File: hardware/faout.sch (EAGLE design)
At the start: 163 parts, among them IC2 MT48LC8M16A2, Q1 L7912ACV, Q2 12MHz, Q3 MUN2214T1, Q4 MUN2214T1, Q5 ASFL, SW1 SMD_TACT_SWITCH, SW2 SMD_TACT_SWITCH, SW3 SMD_TACT_SWITCH, U1 93LC46BT-I/OT, U10 DAC8811DGK, U11 REF102AU, U12 DAC8811DGK, U13 ADR435ARZ, U14 AD8627AKSZ-R2, U15 OPA2277UA/2K5E4, U16 OPA2277UA/2K5E4, U17 MCP1700T-2502E/TT, U18 AD7980ARMZ, U2 LM3480IM3-3.3, U3 LM2940T-12.0, U4 LM3671MF-3.3, U5 LM3671MF-1.2, U6 FLASH-SPI-25XXSMD1, U7 6SLX9TQG144, U8 AD8220ARMZ, U9 REF102AU

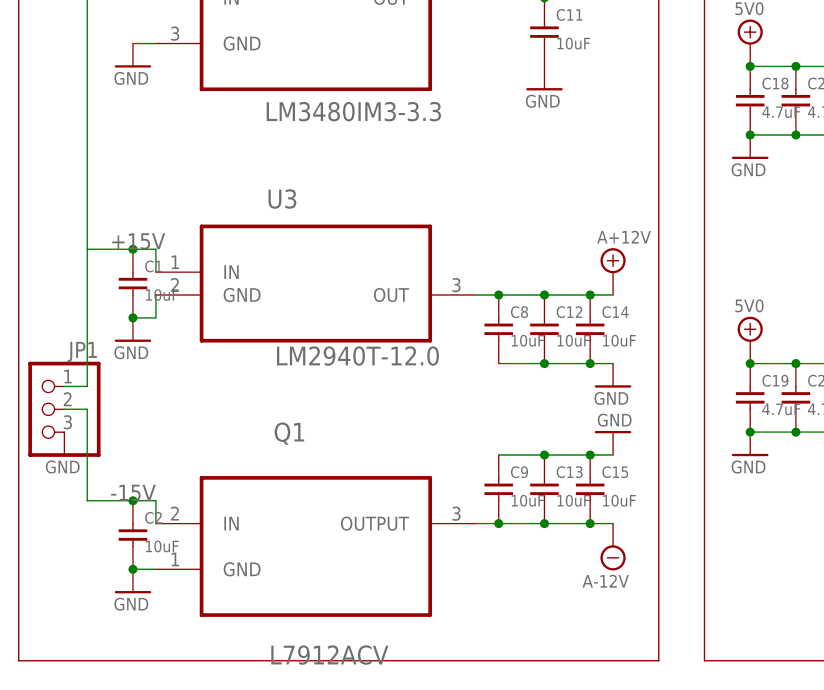
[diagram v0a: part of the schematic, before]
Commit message: Unify analog regulators.
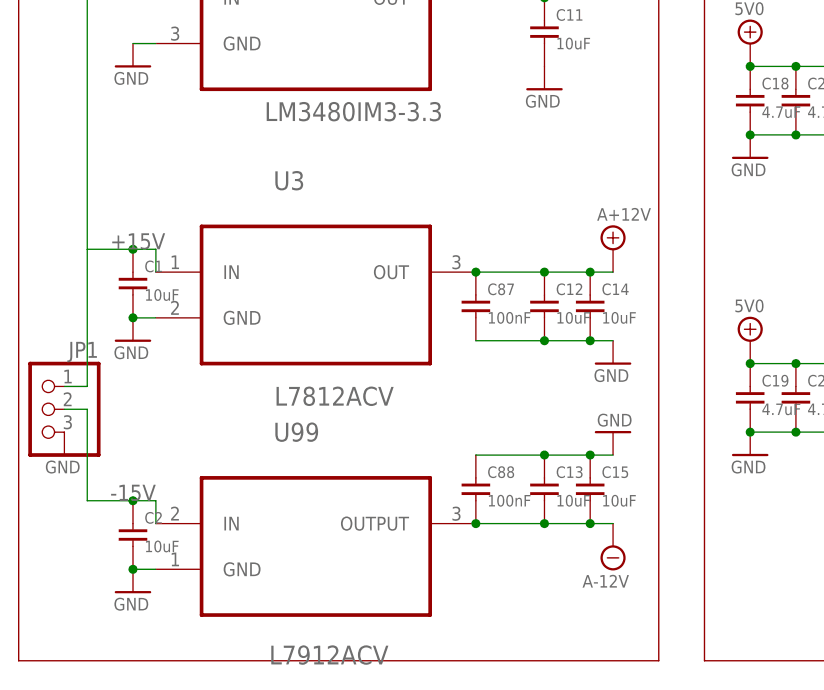
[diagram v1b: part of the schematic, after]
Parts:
- removed C8, C9: 10uF, faout:C_EU0805
- added C87, C88: 100nF, faout:C_EU0603
- U3: value LM2940T-12.0 -> L7812ACV; device faout:LM2940T-12.0 -> faout:L7812ACV
- renumbered Q1 to U99
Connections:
- net A+12V: now also C87.P$1; no longer C8.P$1
- net A-12V: now also C88.P$2; no longer C9.P$2
- net GND: now also C87.P$2, C88.P$1; no longer C8.P$2, C9.P$1
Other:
- moved on the sheet: C12, C14, U3
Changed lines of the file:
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@@
 </part>
 <part name="JP1" library="pinhead" deviceset="PINHD-1X3" device=""/>
-<part name="U3" library="faout" deviceset="LM2940T-12.0" device=""/>
-<part name="Q1" library="faout" deviceset="L7912ACV" device=""/>
+<part name="U3" library="faout" deviceset="L7812ACV" device=""/>
+<part name="U99" library="faout" deviceset="L7912ACV" device=""/>
 <part name="A+12V_PWR7" library="faout" deviceset="A+12V" device=""/>
 <part name="U$1" library="faout" deviceset="A-12V" device=""/>
@@
 <attribute name="OC_FARNELL" value="1867958"/>
 </part>
-<part name="C8" library="faout" deviceset="C_EU" device="0805" value="10uF">
-<attribute name="OC_FARNELL" value="1867958"/>
-</part>
 <part name="C14" library="faout" deviceset="C_EU" device="0805" value="10uF">
 <attribute name="OC_FARNELL" value="1867958"/>
 </part>
-<part name="C9" library="faout" deviceset="C_EU" device="0805" value="10uF">
-<attribute name="OC_FARNELL" value="1867958"/>
-</part>
 <part name="C13" library="faout" deviceset="C_EU" device="0805" value="10uF">
 <attribute name="OC_FARNELL" value="1867958"/>
@@
 <part name="GND_PWR80" library="Bogdan_Commons" deviceset="GND" device=""/>
 <part name="U1" library="faout" deviceset="93LC46BT-I/OT" device=""/>
+<part name="C87" library="faout" deviceset="C_EU" device="0603" value="100nF">
+<attribute name="OC_FARNELL" value="1740621"/>
+</part>
+<part name="C88" library="faout" deviceset="C_EU" device="0603" value="100nF">
+<attribute name="OC_FARNELL" value="1740621"/>
+</part>
 </parts>
 <sheets>
@@
 </instance>
 <instance part="JP1" gate="A" x="-20.32" y="2.54" rot="MR0"/>
-<instance part="U3" gate="A" x="10.16" y="20.32"/>
-<instance part="Q1" gate="A" x="10.16" y="-10.16"/>
-<instance part="A+12V_PWR7" gate="G$1" x="43.18" y="17.78"/>
+<instance part="U3" gate="A" x="10.16" y="17.78"/>
+<instance part="U99" gate="A" x="10.16" y="-10.16"/>
+<instance part="A+12V_PWR7" gate="G$1" x="43.18" y="20.32"/>
 <instance part="U$1" gate="G$1" x="43.18" y="-12.7"/>
 <instance part="GND_PWR13" gate="A" x="-17.78" y="-2.54"/>
 <instance part="GND_PWR75" gate="A" x="-10.16" y="-17.78"/>
 <instance part="GND_PWR76" gate="A" x="-10.16" y="10.16"/>
-<instance part="C12" gate="G$1" x="35.56" y="12.7">
-<attribute name="OC_FARNELL" x="35.56" y="12.7" size="1.778" layer="96" display="off"/>
+<instance part="C12" gate="G$1" x="35.56" y="15.24">
+<attribute name="OC_FARNELL" x="35.56" y="15.24" size="1.778" layer="96" display="off"/>
 </instance>
-<instance part="C8" gate="G$1" x="30.48" y="12.7">
-<attribute name="OC_FARNELL" x="30.48" y="12.7" size="1.778" layer="96" display="off"/>
-</instance>
-<instance part="C14" gate="G$1" x="40.64" y="12.7">
-<attribute name="OC_FARNELL" x="40.64" y="12.7" size="1.778" layer="96" display="off"/>
-</instance>
-<instance part="C9" gate="G$1" x="30.48" y="-5.08">
-<attribute name="OC_FARNELL" x="30.48" y="-5.08" size="1.778" layer="96" display="off"/>
+<instance part="C14" gate="G$1" x="40.64" y="15.24">
+<attribute name="OC_FARNELL" x="40.64" y="15.24" size="1.778" layer="96" display="off"/>
 </instance>
 <instance part="C13" gate="G$1" x="35.56" y="-5.08">
@@
 <attribute name="OC_FARNELL" x="-10.16" y="-10.16" size="1.778" layer="96" display="off"/>
 </instance>
-<instance part="GND_PWR77" gate="A" x="43.18" y="5.08"/>
+<instance part="GND_PWR77" gate="A" x="43.18" y="7.62"/>
 <instance part="GND_PWR78" gate="A" x="43.18" y="0" rot="R180"/>
 <instance part="U2" gate="A" x="10.16" y="48.26"/>
@@
 <instance part="GND_PWR80" gate="A" x="35.56" y="38.1"/>
 <instance part="U1" gate="A" x="-2.54" y="-170.18"/>
+<instance part="C87" gate="G$1" x="27.94" y="15.24">
+<attribute name="OC_FARNELL" x="27.94" y="15.24" size="1.778" layer="96" display="off"/>
+</instance>
+<instance part="C88" gate="G$1" x="27.94" y="-5.08">
+<attribute name="OC_FARNELL" x="27.94" y="-5.08" size="1.778" layer="96" display="off"/>
+</instance>
 </instances>
 <busses>
@@
 </segment>
 <segment>
-<pinref part="Q1" gate="A" pin="GND"/>
+<pinref part="U99" gate="A" pin="GND"/>
 <pinref part="GND_PWR75" gate="A" pin="GND"/>
 <wire x1="-10.16" y1="-15.24" x2="-7.62" y2="-15.24" width="0.1524" layer="91"/>
@@
 <pinref part="GND_PWR76" gate="A" pin="GND"/>
 <wire x1="-10.16" y1="12.7" x2="-7.62" y2="12.7" width="0.1524" layer="91"/>
-<wire x1="-7.62" y1="12.7" x2="-7.62" y2="15.24" width="0.1524" layer="91"/>
 <pinref part="C1" gate="G$1" pin="P$2"/>
 <junction x="-10.16" y="12.7"/>
@@
 <segment>
 <pinref part="GND_PWR78" gate="A" pin="GND"/>
-<pinref part="C9" gate="G$1" pin="P$1"/>
 <wire x1="43.18" y1="-2.54" x2="40.64" y2="-2.54" width="0.1524" layer="91"/>
 <pinref part="C13" gate="G$1" pin="P$1"/>
 <junction x="35.56" y="-2.54"/>
 <wire x1="40.64" y1="-2.54" x2="35.56" y2="-2.54" width="0.1524" layer="91"/>
-<wire x1="35.56" y1="-2.54" x2="30.48" y2="-2.54" width="0.1524" layer="91"/>
+<wire x1="35.56" y1="-2.54" x2="27.94" y2="-2.54" width="0.1524" layer="91"/>
 <pinref part="C15" gate="G$1" pin="P$1"/>
 <junction x="40.64" y="-2.54"/>
+<pinref part="C88" gate="G$1" pin="P$1"/>
 </segment>
 <segment>
-<pinref part="C8" gate="G$1" pin="P$2"/>
 <pinref part="GND_PWR77" gate="A" pin="GND"/>
-<wire x1="30.48" y1="7.62" x2="35.56" y2="7.62" width="0.1524" layer="91"/>
+<wire x1="27.94" y1="10.16" x2="35.56" y2="10.16" width="0.1524" layer="91"/>
 <pinref part="C14" gate="G$1" pin="P$2"/>
-<junction x="40.64" y="7.62"/>
-<wire x1="35.56" y1="7.62" x2="40.64" y2="7.62" width="0.1524" layer="91"/>
-<wire x1="40.64" y1="7.62" x2="43.18" y2="7.62" width="0.1524" layer="91"/>
+<junction x="40.64" y="10.16"/>
+<wire x1="35.56" y1="10.16" x2="40.64" y2="10.16" width="0.1524" layer="91"/>
+<wire x1="40.64" y1="10.16" x2="43.18" y2="10.16" width="0.1524" layer="91"/>
 <pinref part="C12" gate="G$1" pin="P$2"/>
-<junction x="35.56" y="7.62"/>
+<junction x="35.56" y="10.16"/>
+<pinref part="C87" gate="G$1" pin="P$2"/>
 </segment>
 <segment>
@@
 <pinref part="U3" gate="A" pin="OUT"/>
 <pinref part="A+12V_PWR7" gate="G$1" pin="A+12V"/>
-<wire x1="27.94" y1="15.24" x2="30.48" y2="15.24" width="0.1524" layer="91"/>
 <pinref part="C12" gate="G$1" pin="P$1"/>
-<wire x1="30.48" y1="15.24" x2="35.56" y2="15.24" width="0.1524" layer="91"/>
-<wire x1="35.56" y1="15.24" x2="40.64" y2="15.24" width="0.1524" layer="91"/>
-<junction x="35.56" y="15.24"/>
-<pinref part="C8" gate="G$1" pin="P$1"/>
-<junction x="30.48" y="15.24"/>
+<wire x1="27.94" y1="17.78" x2="35.56" y2="17.78" width="0.1524" layer="91"/>
+<wire x1="35.56" y1="17.78" x2="40.64" y2="17.78" width="0.1524" layer="91"/>
+<junction x="35.56" y="17.78"/>
 <pinref part="C14" gate="G$1" pin="P$1"/>
-<wire x1="40.64" y1="15.24" x2="43.18" y2="15.24" width="0.1524" layer="91"/>
-<junction x="40.64" y="15.24"/>
+<wire x1="40.64" y1="17.78" x2="43.18" y2="17.78" width="0.1524" layer="91"/>
+<junction x="40.64" y="17.78"/>
+<pinref part="C87" gate="G$1" pin="P$1"/>
+<junction x="27.94" y="17.78"/>
 </segment>
 </net>
@@
 </segment>
 <segment>
-<pinref part="Q1" gate="A" pin="OUTPUT"/>
 <pinref part="U$1" gate="G$1" pin="A-12V"/>
-<wire x1="27.94" y1="-10.16" x2="30.48" y2="-10.16" width="0.1524" layer="91"/>
-<pinref part="C9" gate="G$1" pin="P$2"/>
-<wire x1="30.48" y1="-10.16" x2="35.56" y2="-10.16" width="0.1524" layer="91"/>
-<junction x="30.48" y="-10.16"/>
 <pinref part="C13" gate="G$1" pin="P$2"/>
 <wire x1="35.56" y1="-10.16" x2="40.64" y2="-10.16" width="0.1524" layer="91"/>
-<junction x="35.56" y="-10.16"/>
 <pinref part="C15" gate="G$1" pin="P$2"/>
 <wire x1="40.64" y1="-10.16" x2="43.18" y2="-10.16" width="0.1524" layer="91"/>
 <junction x="40.64" y="-10.16"/>
+<pinref part="U99" gate="A" pin="OUTPUT"/>
+<pinref part="C88" gate="G$1" pin="P$2"/>
+<junction x="27.94" y="-10.16"/>
+<wire x1="27.94" y1="-10.16" x2="35.56" y2="-10.16" width="0.1524" layer="91"/>
+<junction x="35.56" y="-10.16"/>
 </segment>
 </net>
@@
 <wire x1="-17.78" y1="2.54" x2="-15.24" y2="2.54" width="0.1524" layer="91"/>
 <wire x1="-15.24" y1="2.54" x2="-15.24" y2="-7.62" width="0.1524" layer="91"/>
-<pinref part="Q1" gate="A" pin="IN"/>
+<pinref part="U99" gate="A" pin="IN"/>
 <wire x1="-15.24" y1="-7.62" x2="-10.16" y2="-7.62" width="0.1524" layer="91"/>
 <wire x1="-10.16" y1="-7.62" x2="-7.62" y2="-7.62" width="0.1524" layer="91"/>

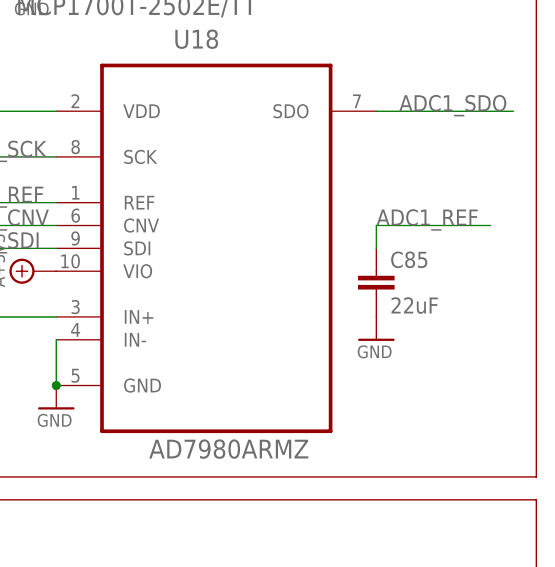
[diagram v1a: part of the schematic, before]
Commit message: Rearrange labels
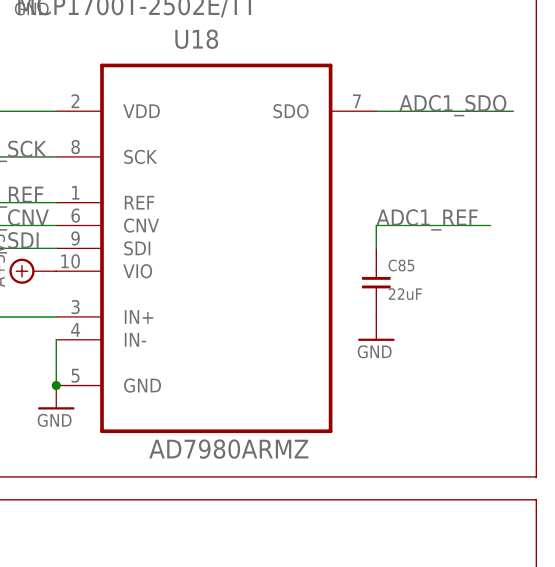
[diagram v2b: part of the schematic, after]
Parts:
- C85: device resistor:C-EUC1206 -> faout:C_EU1206
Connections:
- net ADC1_REF: now also C85.P$1; no longer C85.1
- net GND: now also C85.P$2; no longer C85.2
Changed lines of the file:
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@@
 <part name="U17" library="faout" deviceset="MCP1700T-2502E/TT" device=""/>
 <part name="AI1" library="analog_out_lib" deviceset="BU-SMA" device=""/>
-<part name="C85" library="resistor" deviceset="C-EU" device="C1206" value="22uF"/>
+<part name="C85" library="faout" deviceset="C_EU" device="1206" value="22uF"/>
 <part name="GND_PWR48" library="faout" deviceset="GND" device=""/>
 <part name="GND_PWR49" library="faout" deviceset="GND" device=""/>
@@
 </segment>
 <segment>
-<pinref part="C85" gate="G$1" pin="2"/>
+<pinref part="C85" gate="G$1" pin="P$2"/>
 <pinref part="GND_PWR52" gate="A" pin="GND"/>
 </segment>
@@
 <wire x1="495.3" y1="-83.82" x2="482.6" y2="-83.82" width="0.1524" layer="91"/>
 <label x="482.6" y="-83.82" size="1.778" layer="95"/>
-<pinref part="C85" gate="G$1" pin="1"/>
+<pinref part="C85" gate="G$1" pin="P$1"/>
 <wire x1="482.6" y1="-86.36" x2="482.6" y2="-83.82" width="0.1524" layer="91"/>
 </segment>

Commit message: Cleanup and last adjustments.
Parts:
- removed C87, C88: 100nF, faout:C_EU0603
- removed Q5: ASFL, crystal:ASFL
- removed U99: L7912ACV, faout:L7912ACV
- added C8: 4.7uF, faout:C_EU0603
- added C9: 100nF, faout:C_EU0603
- added PWRLED1: (no value), led:LEDSML0805
- added Q1: 12MHz, faout:TXC_QUARTZ_7A
- added R30: 2k, faout:R_EU0603
- added U19: AD7980ARMZ, faout:AD7980ARMZ
- C6: value 4.7uF -> 100nF; OC_FARNELL 1833803 -> 1740621
- IC1: OC_FARNELL (none) -> 1697461
- Q2: value 12MHz -> MUN2214T1; device faout:TXC_QUARTZ_7A -> transistor-npn:MUN2214T1; OC_FARNELL 1841940 -> 2317629
- Q4: value MUN2214T1 -> ASFL; device transistor-npn:MUN2214T1 -> crystal:ASFL; OC_FARNELL 2317629 -> (none)
- R10: value 100 -> 4.7k
- R17: value 10k -> 100
- R20: value 300 -> 10k
- R25: value 7.47k -> 300
- R27: value 134k -> 7.47k
- R28: value 2k -> 134k
- R7: value 0 -> 300
- R9: value 4.7k -> 0
- U10, U12: value DAC8811DGK -> REF102AU; device faout:DAC8811DGK -> faout:REF102AU
- U11: value REF102AU -> DAC8811DGK; device faout:REF102AU -> faout:DAC8811DGK
- U13: value ADR435ARZ -> DAC8811DGK; device faout:ADR435ARZ -> faout:DAC8811DGK
- U14: value AD8627AKSZ-R2 -> ADR435ARZ; device faout:AD8627AKSZ-R2 -> faout:ADR435ARZ
- U15: value OPA2277UA/2K5E4 -> AD8627AKSZ-R2; device faout:OPA2277UA/2K5E4 -> faout:AD8627AKSZ-R2
- U17: value MCP1700T-2502E/TT -> OPA2277UA/2K5E4; device faout:MCP1700T-2502E/TT -> faout:OPA2277UA/2K5E4
- U18: value AD7980ARMZ -> MCP1700T-2502E/TT; device faout:AD7980ARMZ -> faout:MCP1700T-2502E/TT
- U4: value LM3671MF-3.3 -> L7912ACV; device faout:LM3671MF-3.3 -> faout:L7912ACV
- U5: value LM3671MF-1.2 -> LM3671MF-3.3; device faout:LM3671MF-1.2 -> faout:LM3671MF-3.3
- U6: value FLASH-SPI-25XXSMD1 -> LM3671MF-1.2; device GadgetFactory:FLASH-SPI-25XXSMD1 -> faout:LM3671MF-1.2
- U7: value 6SLX9TQG144 -> M25PE16; device faout:6SLX9TQG144 -> faout:M25PE16; OC_FARNELL 1876228 -> (none)
- U8: value AD8220ARMZ -> 6SLX9TQG144; device faout:AD8220ARMZ -> faout:6SLX9TQG144; OC_FARNELL (none) -> 1876228
- U9: value REF102AU -> AD8220ARMZ; device faout:REF102AU -> faout:AD8220ARMZ
- renumbered JP1 to PWR1, JP2 to USB_RST, JP3 to JTAG, JP4 to RST, JP5 to P1
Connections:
- new net N$26: PWRLED1.C, R7.P$2
- net !DAC1_CS: now also U11.!CS, U8B1.IO_L40N_GCLK10_1; no longer U10.!CS, U7B1.IO_L40N_GCLK10_1
- net !DAC2_CS: now also U13.!CS, U8B1.IO_L42P_GCLK7_1; no longer U12.!CS, U7B1.IO_L42P_GCLK7_1
- net !RAM_CAS: now also U8B3.IO_L52N_3; no longer U7B3.IO_L52N_3
- net !RAM_RAS: now also U8B3.IO_L83P_3; no longer U7B3.IO_L83P_3
- net !RAM_WE: now also U8B3.IO_L52P_3; no longer U7B3.IO_L52P_3
- net !USB_OE: now also U8B0.IO_L64N_SCP4_0; no longer U7B0.IO_L64N_SCP4_0
- net !USB_RD: now also U8B0.IO_L63P_SCP7_0; no longer U7B0.IO_L63P_SCP7_0
- net !USB_RXF: now also U8B0.IO_L62P_0; no longer U7B0.IO_L62P_0
- net !USB_TXE: now also U8B0.IO_L62N_VREF_0; no longer U7B0.IO_L62N_VREF_0
- net !USB_WR: now also U8B0.IO_L63N_SCP6_0; no longer U7B0.IO_L63N_SCP6_0
- net -15V: now also U4.IN; no longer U99.IN
- net 1V2: now also U6.FB, U8BVCCINT.VCCINT@0, U8BVCCINT.VCCINT@1, U8BVCCINT.VCCINT@2, U8BVCCINT.VCCINT@3, U8BVCCINT.VCCINT@4; no longer U5.FB, U7BVCCINT.VCCINT@0, U7BVCCINT.VCCINT@1, U7BVCCINT.VCCINT@2, U7BVCCINT.VCCINT@3, U7BVCCINT.VCCINT@4
- net 2V5: now also U18.VOUT, U19.VDD; no longer U17.VOUT, U18.VDD
- net 3V3: now also C9.P$1, PWRLED1.A, Q4.OE, Q4.VCC, R10.P$2, R20.P$2, U5.FB, U6.EN, U7.!RESET, U7.!WP, U7.VCC, U8B0.VCCO_0@0, U8B0.VCCO_0@1, U8B0.VCCO_0@2, U8B1.VCCO_1@0, U8B1.VCCO_1@1, U8B1.VCCO_1@2, U8B2.IO_L1N_M0_CMPMISO_2, U8B2.VCCO_2@0, U8B2.VCCO_2@1, U8B3.VCCO_3@0, U8B3.VCCO_3@1, U8B3.VCCO_3@2, U8BVCCAUX.VCCAUX@0, U8BVCCAUX.VCCAUX@1, U8BVCCAUX.VCCAUX@2, U8BVCCAUX.VCCAUX@3, U8BVCCAUX.VCCAUX@4; no longer C7.P$1, Q5.OE, Q5.VCC, R17.P$2, R9.P$2, U4.FB, U5.EN, U6.HOLD, U6.VCC, U6.WP, U7B0.VCCO_0@0, U7B0.VCCO_0@1, U7B0.VCCO_0@2, U7B1.VCCO_1@0, U7B1.VCCO_1@1, U7B1.VCCO_1@2, U7B2.IO_L1N_M0_CMPMISO_2, U7B2.VCCO_2@0, U7B2.VCCO_2@1, U7B3.VCCO_3@0, U7B3.VCCO_3@1, U7B3.VCCO_3@2, U7BVCCAUX.VCCAUX@0, U7BVCCAUX.VCCAUX@1, U7BVCCAUX.VCCAUX@2, U7BVCCAUX.VCCAUX@3, U7BVCCAUX.VCCAUX@4
- net 5V0: now also R8.P$1, U5.EN, U6.VIN; no longer R7.P$1, U4.EN, U4.VIN
- net A+12V: now also C6.P$1, U14.VIN, U17.V+, U9.+VS; no longer C87.P$1, U13.VIN, U14.V+, U8.+VS
- net A+3V3: now also U10.V+, U11.VDD, U12.V+, U13.VDD, U18.VIN, U19.VIO; no longer U10.VDD, U11.V+, U12.VDD, U17.VIN, U18.VIO, U9.V+
- net A-12V: now also C7.P$2, U17.V-, U4.OUTPUT, U9.-VS; no longer C88.P$2, U14.V-, U8.-VS, U99.OUTPUT
- net ADC1_CNV: now also U19.CNV, U8B1.IO_L33P_1; no longer U18.CNV, U7B1.IO_L33P_1
- net ADC1_REF: now also U14.VOUT, U19.REF; no longer U13.VOUT, U18.REF
- net ADC1_SCK: now also U19.SCK, U8B1.IO_L34P_1; no longer U18.SCK, U7B1.IO_L34P_1
- net ADC1_SDI: now also U19.SDI, U8B1.IO_L34N_1; no longer U18.SDI, U7B1.IO_L34N_1
- net ADC1_SDO: now also U19.SDO, U8B1.IO_L33N_1; no longer U18.SDO, U7B1.IO_L33N_1
- net BUTTON1: now also U8B2.IO_L12N_D2_MISO3_2; no longer U7B2.IO_L12N_D2_MISO3_2
- net BUTTON2: now also U8B2.IO_L12P_D1_MISO2_2; no longer U7B2.IO_L12P_D1_MISO2_2
- net BUTTON3: now also U8B2.IO_L2N_CMPMOSI_2; no longer U7B2.IO_L2N_CMPMOSI_2
- net CLK_IN: now also Q4.FO, U8B1.IO_L40P_GCLK11_1; no longer Q5.FO, U7B1.IO_L40P_GCLK11_1
- net DAC1_CLK: now also U11.CLK, U8B1.IO_L41P_GCLK9_IRDY1_1; no longer U10.CLK, U7B1.IO_L41P_GCLK9_IRDY1_1
- net DAC1_IOUT: now also U11.IOUT, U17.-IN_A; no longer U10.IOUT, U16.-IN_A
- net DAC1_SDI: now also U11.SDI, U8B1.IO_L41N_GCLK8_1; no longer U10.SDI, U7B1.IO_L41N_GCLK8_1
- net DAC1_VOUT: now also U11.RFB, U17.OUT_A; no longer U10.RFB, U16.OUT_A
- net DAC1_VREF: now also U10.COM, U11.VREF, U17.OUT_B; no longer U10.VREF, U16.OUT_B, U9.COM
- net DAC1_VREFOUT: now also R29.P$2, U17.-IN_B; no longer R28.P$2, U16.-IN_B
- net DAC2_CLK: now also U13.CLK, U8B1.IO_L42N_GCLK6_TRDY1_1; no longer U12.CLK, U7B1.IO_L42N_GCLK6_TRDY1_1
- net DAC2_IOUT: now also U13.IOUT, U16.-IN_A; no longer U12.IOUT, U15.-IN_A
- net DAC2_SDI: now also U13.SDI, U8B1.IO_L43P_GCLK5_1; no longer U12.SDI, U7B1.IO_L43P_GCLK5_1
- net DAC2_VOUT: now also U13.RFB, U16.OUT_A; no longer U12.RFB, U15.OUT_A
- net DAC2_VREF: now also U12.COM, U13.VREF, U16.OUT_B; no longer U11.COM, U12.VREF, U15.OUT_B
- net DAC2_VREFOUT: now also R30.P$2, U16.-IN_B; no longer R29.P$2, U15.-IN_B
- net DISP_A: now also R11.P$2, U8B2.IO_L30N_GCLK0_USERCCLK_2; no longer R10.P$2, U7B2.IO_L30N_GCLK0_USERCCLK_2
- net DISP_B: now also R12.P$2, U8B2.IO_L30P_GCLK1_D13_2; no longer R11.P$2, U7B2.IO_L30P_GCLK1_D13_2
- net DISP_C: now also R13.P$2, U8B2.IO_L48P_D7_2; no longer R12.P$2, U7B2.IO_L48P_D7_2
- net DISP_CAT1: now also Q3.C; no longer Q4.C
- net DISP_D: now also R14.P$2, U8B2.IO_L31N_GCLK30_D15_2; no longer R13.P$2, U7B2.IO_L31N_GCLK30_D15_2
- net DISP_E: now also R15.P$2, U8B2.IO_L48N_RDWR_B_VREF_2; no longer R14.P$2, U7B2.IO_L48N_RDWR_B_VREF_2
- net DISP_EN1: now also Q3.B, U8B2.IO_L14P_D11_2; no longer Q4.B, U7B2.IO_L14P_D11_2
- net DISP_EN2: now also Q2.B, U8B2.IO_L13N_D10_2; no longer Q3.B, U7B2.IO_L13N_D10_2
- net DISP_F: now also R16.P$2, U8B2.IO_L31P_GCLK31_D14_2; no longer R15.P$2, U7B2.IO_L31P_GCLK31_D14_2
- net DISP_G: now also R17.P$2, U8B2.IO_L14N_D12_2; no longer R16.P$2, U7B2.IO_L14N_D12_2
- net DISP_INT_A: now also R11.P$1; no longer R10.P$1
- net DISP_INT_B: now also R12.P$1; no longer R11.P$1
- net DISP_INT_C: now also R13.P$1; no longer R12.P$1
- net DISP_INT_D: now also R14.P$1; no longer R13.P$1
- net DISP_INT_E: now also R15.P$1; no longer R14.P$1
- net DISP_INT_F: now also R16.P$1; no longer R15.P$1
- net DISP_INT_G: now also R17.P$1; no longer R16.P$1
- net FLASH_CS: now also U7.!CS, U8B2.IO_L65N_CSO_B_2; no longer U6.CS, U7B2.IO_L65N_CSO_B_2
- net FLASH_MISO: now also U7.SDO, U8B2.IO_L3P_D0_DIN_MISO_MISO1_2; no longer U6.MISO, U7B2.IO_L3P_D0_DIN_MISO_MISO1_2
- net FLASH_MOSI: now also U7.SDI, U8B2.IO_L3N_MOSI_CSI_B_MISO0_2; no longer U6.MOSI, U7B2.IO_L3N_MOSI_CSI_B_MISO0_2
- net FLASH_SCK: now also U7.SCK, U8B2.IO_L1P_CCLK_2; no longer U6.SCK, U7B2.IO_L1P_CCLK_2
- net GND: now also C7.P$1, C8.P$2, C9.P$2, Q2.E, Q4.GND, R25.P$1, R27.P$1, R7.P$1, R9.P$1, U11.GND, U14.GND, U17.+IN_A, U17.+IN_B, U19.GND, U19.IN-, U7.GND, U8B0.IO_L1P_HSWAPEN_0, U8B2.IO_L13P_M1_2, U8BGND.GND@0, U8BGND.GND@1, U8BGND.GND@10, U8BGND.GND@11, U8BGND.GND@12, U8BGND.GND@2, U8BGND.GND@3, U8BGND.GND@4, U8BGND.GND@5, U8BGND.GND@6, U8BGND.GND@7, U8BGND.GND@8, U8BGND.GND@9, U8BNA.SUSPEND, U9.REF; no longer C7.P$2, C87.P$2, C88.P$1, Q4.E, Q5.GND, R20.P$1, R26.P$1, R8.P$1, U10.GND, U12.GND, U15.+IN_A, U15.+IN_B, U17.GND, U18.IN-, U7B0.IO_L1P_HSWAPEN_0, U7B2.IO_L13P_M1_2, U7BGND.GND@0, U7BGND.GND@1, U7BGND.GND@10, U7BGND.GND@11, U7BGND.GND@12, U7BGND.GND@2, U7BGND.GND@3, U7BGND.GND@4, U7BGND.GND@5, U7BGND.GND@6, U7BGND.GND@7, U7BGND.GND@8, U7BGND.GND@9, U7BNA.SUSPEND, U8.REF, U99.GND
- net JP_1: now also U8B1.IO_L43N_GCLK4_1; no longer U7B1.IO_L43N_GCLK4_1
- net JP_2: now also U8B1.IO_L45P_1; no longer U7B1.IO_L45P_1
- net JP_3: now also U8B1.IO_L45N_1; no longer U7B1.IO_L45N_1
- net JP_4: now also U8B1.IO_L46P_1; no longer U7B1.IO_L46P_1
- net LED1: now also U8B1.IO_L46N_1; no longer U7B1.IO_L46N_1
- net LED2: now also U8B1.IO_L47P_1; no longer U7B1.IO_L47P_1
- net LED3: now also U8B1.IO_L47N_1; no longer U7B1.IO_L47N_1
- net LED_4: now also U8B0.IO_L66P_SCP1_0; no longer U7B0.IO_L66P_SCP1_0
- net LED_5: now also U8B0.IO_L66N_SCP0_0; no longer U7B0.IO_L66N_SCP0_0
- net N$1: now also Q1.P$1; no longer Q2.P$1
- net N$10: now also R29.P$1, U10.VOUT; no longer R28.P$1, U9.VOUT
- net N$11: now also U9.-IN; no longer U8.-IN
- net N$12: now also U15.-IN, U15.OUT_A, U19.IN+; no longer U14.-IN, U14.OUT_A, U18.IN+
- net N$13: now also R26.P$2, U9.VOUT; no longer R25.P$2, U8.VOUT
- net N$14: now also R26.P$1, R27.P$2, R28.P$1; no longer R25.P$1, R26.P$2, R27.P$1
- net N$15: now also R28.P$2, U15.+IN; no longer R27.P$2, U14.+IN
- net N$17: now also Q2.C; no longer Q3.C
- net N$18: now also R18.P$1; no longer R17.P$1
- net N$19: now also R19.P$1; no longer R18.P$1
- net N$2: now also Q1.P$2; no longer Q2.P$2
- net N$20: now also R20.P$1; no longer R19.P$1
- net N$21: now also R21.P$2; no longer R20.P$2
- net N$22: now also R22.P$2; no longer R21.P$2
- net N$23: now also R23.P$2; no longer R22.P$2
- net N$24: now also U5.SW; no longer U4.SW
- net N$25: now also U6.SW; no longer U5.SW
- net N$3: now also R24.P$2; no longer R23.P$2
- net N$4: now also R25.P$2; no longer R24.P$2
- net N$5: now also C8.P$1; no longer C6.P$1
- net N$8: now also R30.P$1, U12.VOUT; no longer R29.P$1, U11.VOUT
- net N$9: now also U9.+IN; no longer U8.+IN
- net RAM_A0: now also U8B0.IO_L3P_0; no longer U7B0.IO_L3P_0
- net RAM_A1: now also U8B0.IO_L3N_0; no longer U7B0.IO_L3N_0
- net RAM_A10: now also U8B0.IO_L2N_0; no longer U7B0.IO_L2N_0
- net RAM_A11: now also U8B3.IO_L1P_3; no longer U7B3.IO_L1P_3
- net RAM_A2: now also U8B0.IO_L4P_0; no longer U7B0.IO_L4P_0
- net RAM_A3: now also U8B0.IO_L4N_0; no longer U7B0.IO_L4N_0
- net RAM_A4: now also U8B2.IO_L49P_D3_2; no longer U7B2.IO_L49P_D3_2
- net RAM_A5: now also U8B2.IO_L49N_D4_2; no longer U7B2.IO_L49N_D4_2
- net RAM_A6: now also U8B2.IO_L62P_D5_2; no longer U7B2.IO_L62P_D5_2
- net RAM_A7: now also U8B2.IO_L62N_D6_2; no longer U7B2.IO_L62N_D6_2
- net RAM_A8: now also U8B2.IO_L64P_D8_2; no longer U7B2.IO_L64P_D8_2
- net RAM_A9: now also U8B2.IO_L64N_D9_2; no longer U7B2.IO_L64N_D9_2
- net RAM_BA0: now also U8B0.IO_L1N_VREF_0; no longer U7B0.IO_L1N_VREF_0
- net RAM_BA1: now also U8B0.IO_L2P_0; no longer U7B0.IO_L2P_0
- net RAM_CKE: now also U8B3.IO_L2P_3; no longer U7B3.IO_L2P_3
- net RAM_CLK: now also U8B3.IO_L2N_3; no longer U7B3.IO_L2N_3
- net RAM_CS: now also U8B3.IO_L83N_VREF_3; no longer U7B3.IO_L83N_VREF_3
- net RAM_DQ0: now also U8B3.IO_L50N_3; no longer U7B3.IO_L50N_3
- net RAM_DQ1: now also U8B3.IO_L50P_3; no longer U7B3.IO_L50P_3
- net RAM_DQ10: now also U8B3.IO_L41N_GCLK26_3; no longer U7B3.IO_L41N_GCLK26_3
- net RAM_DQ11: now also U8B3.IO_L41P_GCLK27_3; no longer U7B3.IO_L41P_GCLK27_3
- net RAM_DQ12: now also U8B3.IO_L37N_3; no longer U7B3.IO_L37N_3
- net RAM_DQ13: now also U8B3.IO_L37P_3; no longer U7B3.IO_L37P_3
- net RAM_DQ14: now also U8B3.IO_L36N_3; no longer U7B3.IO_L36N_3
- net RAM_DQ15: now also U8B3.IO_L36P_3; no longer U7B3.IO_L36P_3
- net RAM_DQ2: now also U8B3.IO_L49N_3; no longer U7B3.IO_L49N_3
- net RAM_DQ3: now also U8B3.IO_L49P_3; no longer U7B3.IO_L49P_3
- net RAM_DQ4: now also U8B3.IO_L44N_GCLK20_3; no longer U7B3.IO_L44N_GCLK20_3
- net RAM_DQ5: now also U8B3.IO_L44P_GCLK21_3; no longer U7B3.IO_L44P_GCLK21_3
- net RAM_DQ6: now also U8B3.IO_L43N_GCLK22_IRDY2_3; no longer U7B3.IO_L43N_GCLK22_IRDY2_3
- net RAM_DQ7: now also U8B3.IO_L51P_3; no longer U7B3.IO_L51P_3
- net RAM_DQ8: now also U8B3.IO_L42N_GCLK24_3; no longer U7B3.IO_L42N_GCLK24_3
- net RAM_DQ9: now also U8B3.IO_L42P_GCLK25_TRDY2_3; no longer U7B3.IO_L42P_GCLK25_TRDY2_3
- net RAM_DQMH: now also U8B3.IO_L43P_GCLK23_3; no longer U7B3.IO_L43P_GCLK23_3
- net RAM_DQML: now also U8B3.IO_L51N_3; no longer U7B3.IO_L51N_3
- net RESET: now also R10.P$1, U8B2.PROGRAM_B_2; no longer R9.P$1, U7B2.PROGRAM_B_2
- net TCK: now also U8BNA.TCK; no longer U7BNA.TCK
- net TDI: now also U8BNA.TDI; no longer U7BNA.TDI
- net TDO: now also U8BNA.TDO; no longer U7BNA.TDO
- net TMS: now also U8BNA.TMS; no longer U7BNA.TMS
- net USB_CLKOUT: now also U8B0.IO_L37N_GCLK12_0; no longer U7B0.IO_L37N_GCLK12_0
- net USB_D0: now also U8B0.IO_L64P_SCP5_0; no longer U7B0.IO_L64P_SCP5_0
- net USB_D1: now also U8B0.IO_L34P_GCLK19_0; no longer U7B0.IO_L34P_GCLK19_0
- net USB_D2: now also U8B0.IO_L34N_GCLK18_0; no longer U7B0.IO_L34N_GCLK18_0
- net USB_D3: now also U8B0.IO_L35P_GCLK17_0; no longer U7B0.IO_L35P_GCLK17_0
- net USB_D4: now also U8B0.IO_L35N_GCLK16_0; no longer U7B0.IO_L35N_GCLK16_0
- net USB_D5: now also U8B0.IO_L36P_GCLK15_0; no longer U7B0.IO_L36P_GCLK15_0
- net USB_D6: now also U8B0.IO_L36N_GCLK14_0; no longer U7B0.IO_L36N_GCLK14_0
- net USB_D7: now also U8B0.IO_L37P_GCLK13_0; no longer U7B0.IO_L37P_GCLK13_0
- net USB_GND: now also R9.P$2; no longer R8.P$2
- net USB_V: now also R8.P$2; no longer R7.P$2
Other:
- moved on the sheet: C6, C7, Q3, R10, R11, R12, R13, R14, R15, R16, R17, R18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

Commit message: Fix display orientation and start production.
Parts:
- C37, C39, C59: OC_FARNELL (none) -> 1759102
- C50: OC_FARNELL (none) -> 1867949
- C67, C69, C84, C86: OC_FARNELL (none) -> 1759409
- C85: OC_FARNELL (none) -> 1833823
- R5: value 1k -> 10k
- renumbered DISP1 to DISP, PWR1 to APWR, PWRLED1 to PWR
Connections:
- net N$17 renamed DISP_CAT2
- net DISP_A: now also R14.P$2, U8B2.IO_L31N_GCLK30_D15_2; no longer R11.P$2, U8B2.IO_L30N_GCLK0_USERCCLK_2
- net DISP_B: now also R13.P$2, U8B2.IO_L48P_D7_2; no longer R12.P$2, U8B2.IO_L30P_GCLK1_D13_2
- net DISP_C: now also R12.P$2, U8B2.IO_L30P_GCLK1_D13_2; no longer R13.P$2, U8B2.IO_L48P_D7_2
- net DISP_D: now also R11.P$2, U8B2.IO_L30N_GCLK0_USERCCLK_2; no longer R14.P$2, U8B2.IO_L31N_GCLK30_D15_2
- net DISP_E: now also R17.P$2, U8B2.IO_L14N_D12_2; no longer R15.P$2, U8B2.IO_L48N_RDWR_B_VREF_2
- net DISP_G: now also R15.P$2, U8B2.IO_L48N_RDWR_B_VREF_2; no longer R17.P$2, U8B2.IO_L14N_D12_2
- net DISP_INT_A: now also R14.P$1; no longer R11.P$1
- net DISP_INT_B: now also R13.P$1; no longer R12.P$1
- net DISP_INT_C: now also R12.P$1; no longer R13.P$1
- net DISP_INT_D: now also R11.P$1; no longer R14.P$1
- net DISP_INT_E: now also R17.P$1; no longer R15.P$1
- net DISP_INT_G: now also R15.P$1; no longer R17.P$1
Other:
- moved on the sheet: R11, R12, R13, R14, R15, R17
